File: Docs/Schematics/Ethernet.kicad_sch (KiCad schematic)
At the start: 22 parts, among them J1 RJ45, J2 SPI, U2 ENC28J60

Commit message: Revision 2
Fixes based after sponsor interview.
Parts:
- added C5: 100nF, symbol Device:C_Small
- added C6, C7: 18pF, symbol Device:C_Small
- added Y1: 25MHz, symbol Device:Crystal_Small
- renumbered C1 to C4
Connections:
- net +3.3V is gone; now on net VDD: L1.2, U2.15 (VDDTX), U2.19 (VDDRX), U2.25 (VDDOSC), U2.28 (VDD)
- net GND: now also U2.21 (VSSPLL), C5.2, C6.1, C7.1; no longer U2.24 (OSC2)
- net VDD: now reaches U2.20 (VDDPLL)
- net VDD: now also C5.1
- net XOSCOUT: no longer names the net of U2.23 (OSC1)
- net XOSCOUT: now also C6.2, Y1.2
- new net: C7.2, U2.24 (OSC2), Y1.1

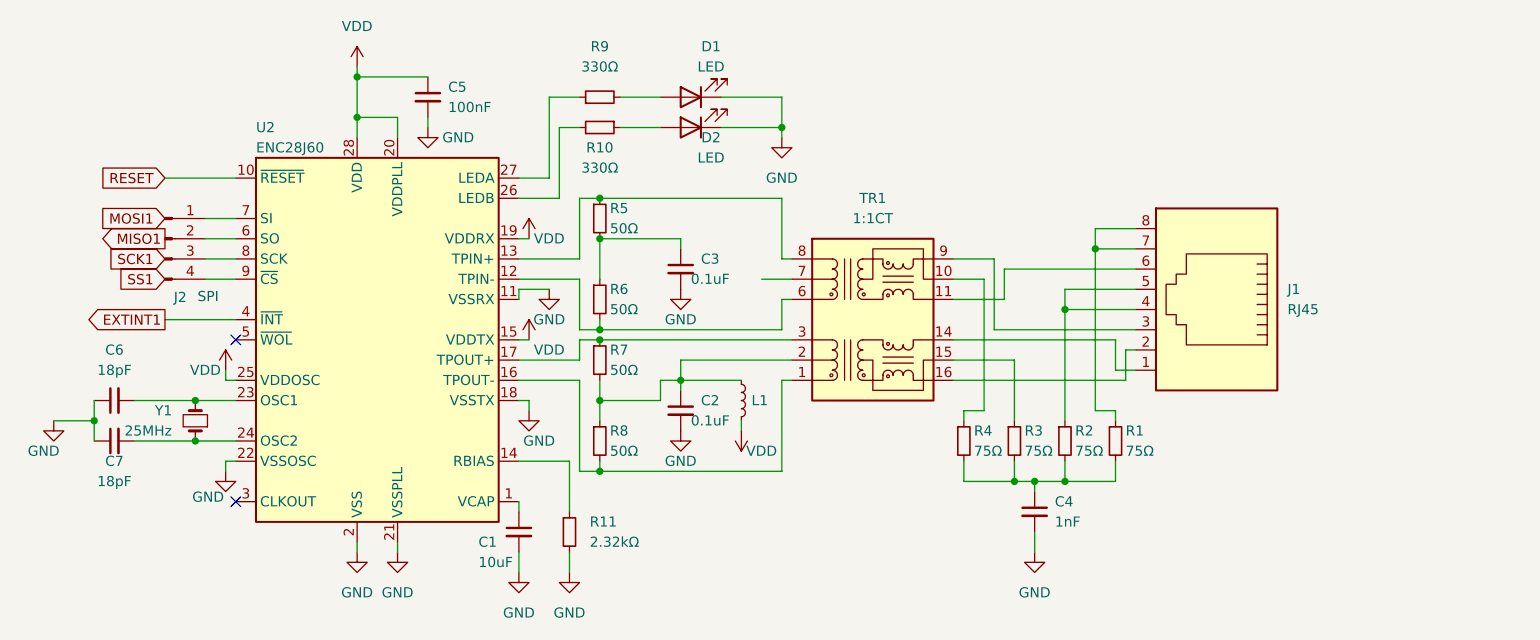
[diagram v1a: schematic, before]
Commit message: Revision 3
Revisions made after meeting with sponsor.
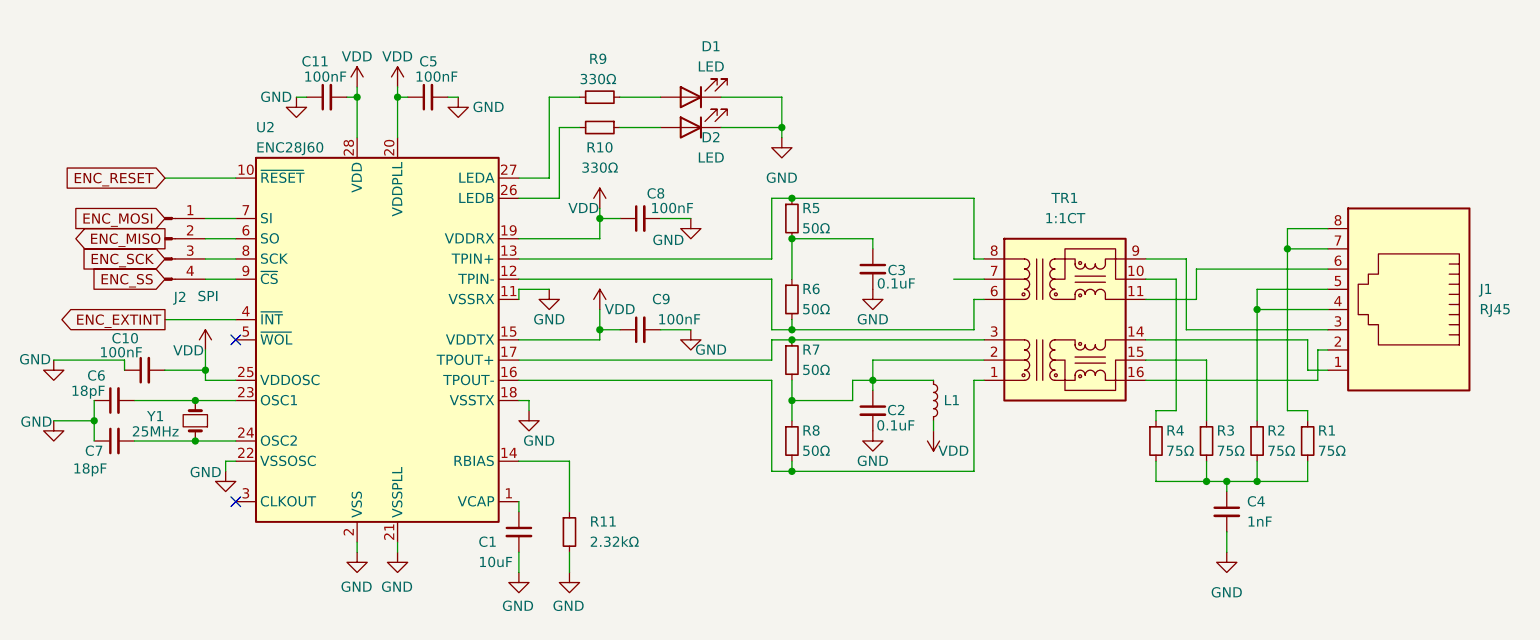
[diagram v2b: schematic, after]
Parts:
- added C10, C11, C8, C9: 100nF, symbol Device:C_Small
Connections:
- net GND: now also C10.1, C11.1, C8.2, C9.2
- net VDD: now also C10.2, C11.2, C8.1, C9.1
- net EXTINT1 renamed ENC_EXTINT
- net RESET renamed ENC_RESET
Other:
- moved on the sheet: C2, C3, C4, C5, J1, L1, R1, R2, R3, R4, R5, R6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
